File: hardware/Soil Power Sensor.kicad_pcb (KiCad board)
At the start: 2 copper layers, 139 x 45 mm, 76 parts, among them J1 Screw_Terminal_01x05, J2 RFShield_OnePiece, J3 UART, J4 Conn_01x03, J5 Micro_SD_Card, J7 Conn_01x04_Socket, Q1 BSS123, SW1 BOOT, SW2 EN, SW3 SW_DP3T, U1 MAX9944, U10 Wio-E5 mini, U2 INA296A, U3 REF2033, U4 THS4532, U5 TPS60400DBV, U6 ADS1219, U7 SN74LVC1G240, U8 ESP32-C3-WROOM-02-N4, U9 FM24CL16B

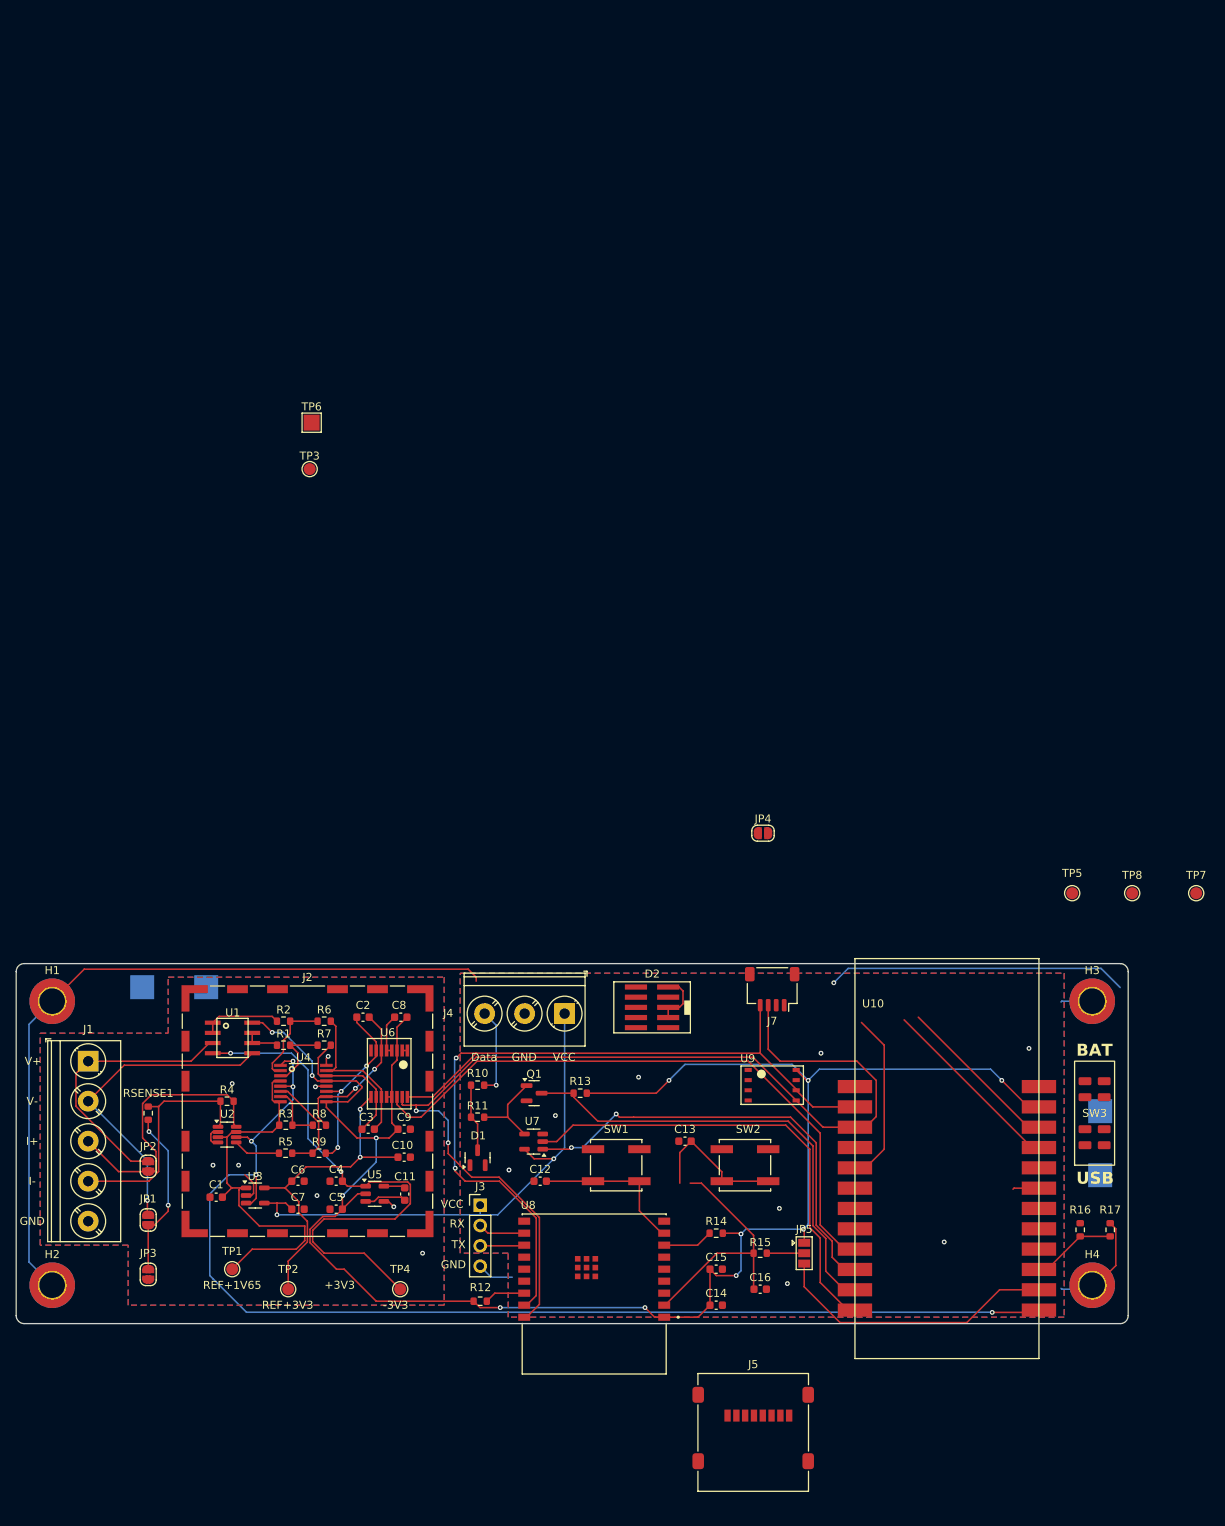
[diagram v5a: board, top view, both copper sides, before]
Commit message: Updated TP locations
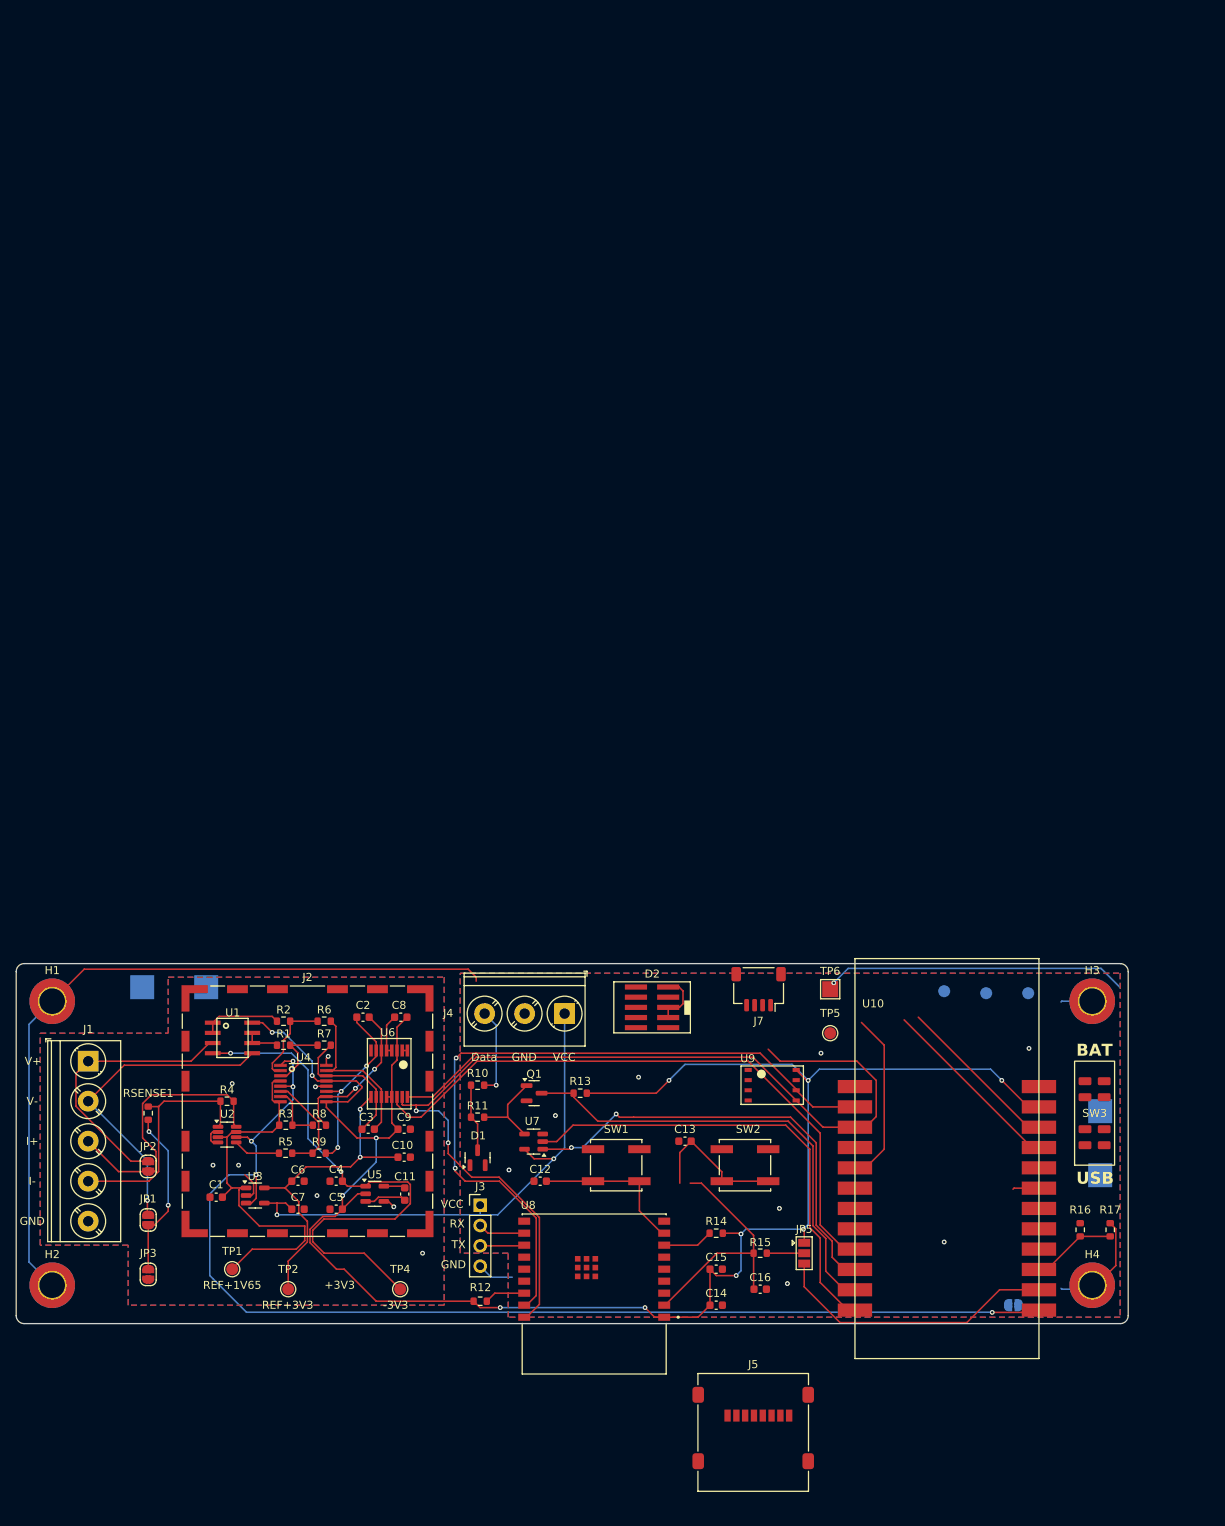
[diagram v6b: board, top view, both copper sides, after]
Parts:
- JP4, TP3, TP7, TP8: moved to B.Cu
- moved TP3 102.7 mm to (228.0, 50.2), turned to 180 degrees
- moved TP6 96.0 mm to (213.8, 50.0)
- moved JP4 66.8 mm to (236.7, 89.5), turned to 180 degrees
- moved TP5 34.9 mm to (213.8, 55.5)
- moved TP7 29.1 mm to (233.2, 50.5)
- moved TP8 18.0 mm to (238.5, 50.5)
- moved J7 1.70 mm to (204.8, 50.0)
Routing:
- net /STM32/SCL: track 108.8 -> 102.8 mm
- net /STM32/SDA: track 129.5 -> 124.0 mm

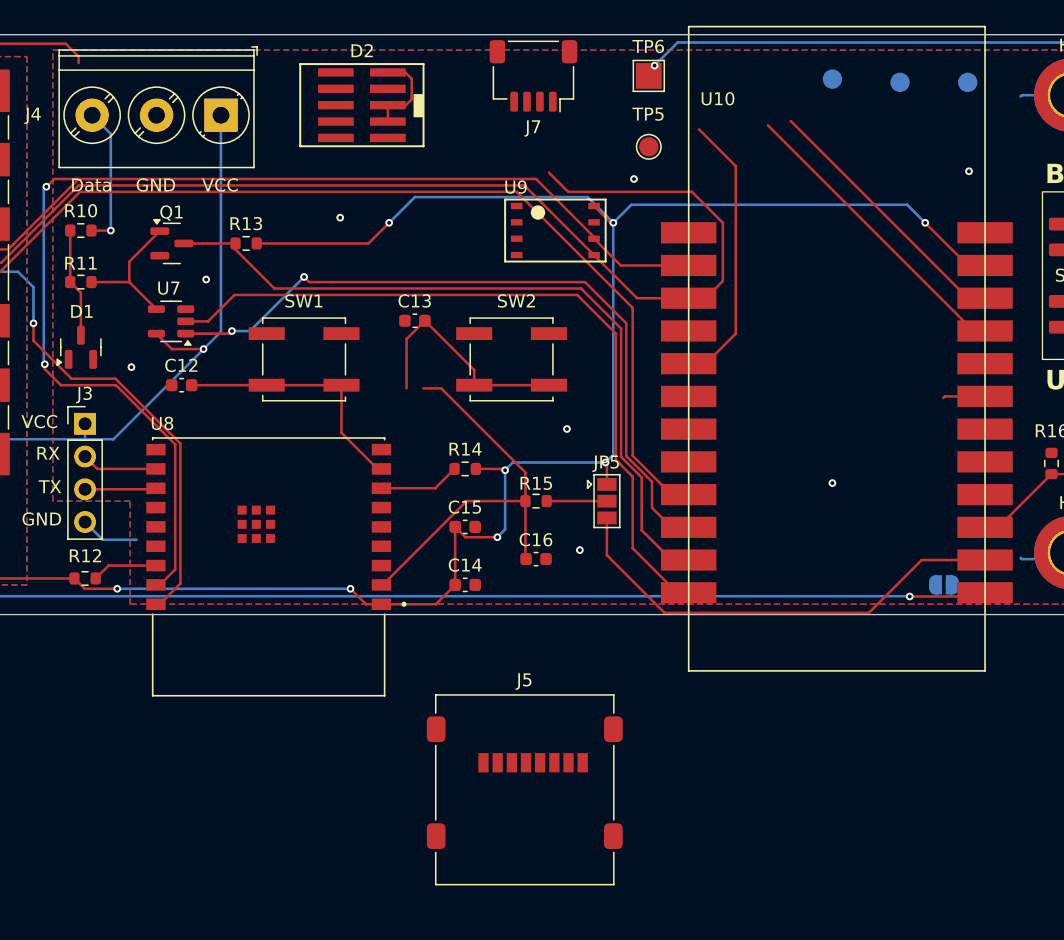
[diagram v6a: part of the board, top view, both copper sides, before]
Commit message: Placed microSD card slot
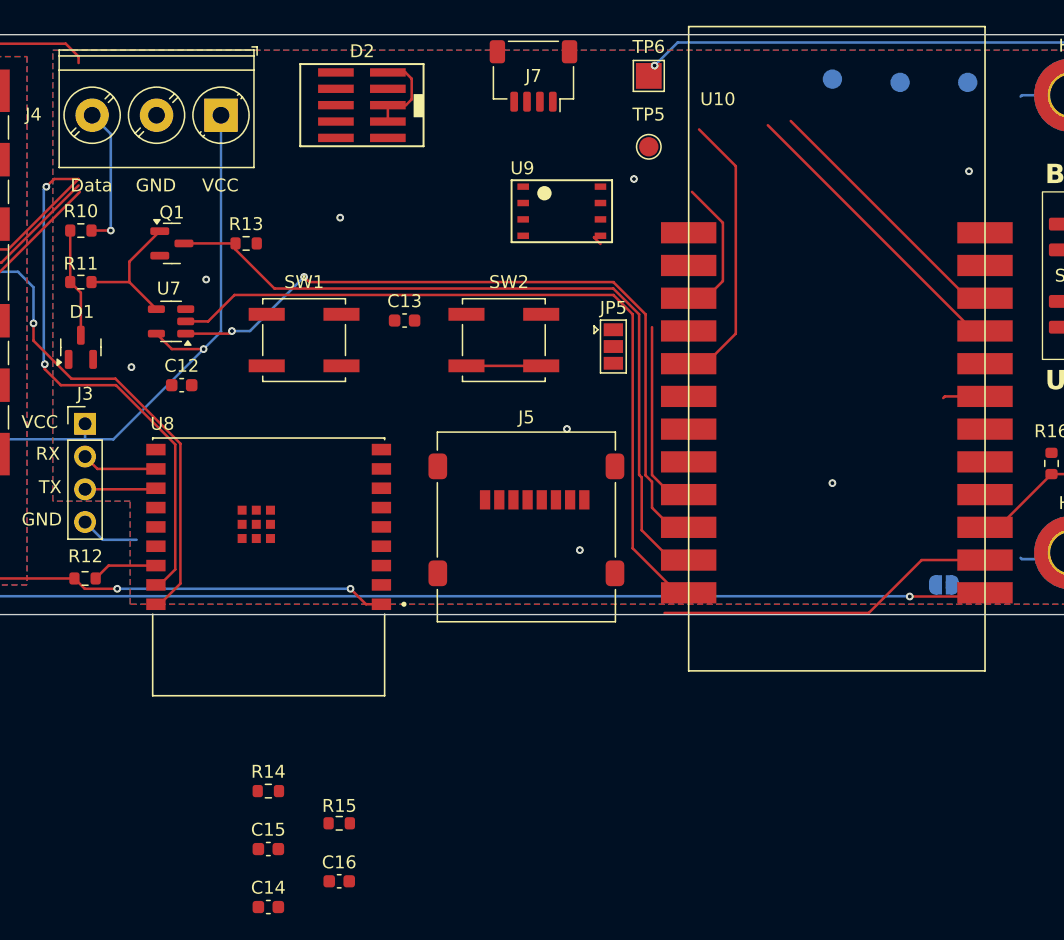
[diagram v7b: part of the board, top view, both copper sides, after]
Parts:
- moved C14 29.3 mm to (184.2, 114.5)
- moved C15 29.3 mm to (184.2, 110.0)
- moved C16 29.3 mm to (189.7, 112.5)
- moved R14 29.3 mm to (184.2, 105.5)
- moved R15 29.3 mm to (189.7, 108.0)
- moved J5 20.4 mm to (204.2, 85.0)
- moved JP5 12.0 mm to (211.0, 71.0)
- moved SW2 1.62 mm to (202.5, 70.5)
- moved U9 1.58 mm to (204.0, 58.6)
- moved SW1 1.50 mm to (187.0, 70.5)
- moved C13 0.80 mm to (194.8, 69.0)
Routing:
- net +3V3: track 234.4 -> 120.1 mm, vias 12 -> 6
- net /STM32/SDA: track 124.0 -> 62.1 mm
- net /STM32/SCL: track 102.8 -> 52.6 mm
- net /Analog/ADC_DRDY: track 78.2 -> 29.5 mm
- net /ESP32/EN: track 49.5 -> 5.87 mm
- net /ESP32/BOOT: track 19.6 -> 0.00 mm
- net /ESP32/ESP32_EN: track 35.8 -> 26.6 mm
- net Net-(U8-IO8): track 6.30 -> 0.00 mm
- net Net-(JP5-C): track 4.68 -> 0.00 mm
- net /STM32/SDI12_TX: track 58.4 -> 60.1 mm
- net /STM32/SDI12_RX: track 57.9 -> 59.3 mm
- net /STM32/SDI12_DIR: track 56.1 -> 57.4 mm

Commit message: Updated FRAM
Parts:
- removed U9: FM24CL16B, Soil Power Sensor:SOIC127P602X164-8N
- added U11: MB85RC1MT, Soil Power Sensor:SOP127P505X155-8N, F.Cu at (207.0, 61.2)
- added U12: MB85RC1MT, Soil Power Sensor:SOP127P505X155-8N, F.Cu at (193.2, 61.3)
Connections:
- J5 pad 9: unconnected-(J5-SHIELD-Pad9) -> GND
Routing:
- net /STM32/SDA: track 62.1 -> 61.3 mm
- net GND: vias 16 -> 15
